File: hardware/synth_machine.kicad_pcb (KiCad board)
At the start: 2 copper layers, 100 x 100 mm, 93 parts, among them J1 USB-C (MIDI + 5V power), J10 Pot WAV (10k lin, panel) JST-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, J11 Pot ATK (10k lin, panel) JST-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, J12 Pot DEC (10k lin, panel) JST-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, J13 Pot SUS (10k lin, panel) JST-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, J14 Pot REL (10k lin, panel) JST-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, J5 Speaker L (JST-PH), J6 Speaker R (JST-PH), J7 Headphones 3.5mm (CUI SJ1-351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, J8 Expansion, K1 KEY C4 (direct D10) JST-XH, K10 A4 [c2 r2] JST-XH, K11 A#4 [c1 r1] JST-XH, K12 B4 [c1 r2] JST-XH, K13 C5 [c0 r2] JST-XH, K14 BTN1 [c0 r0] JST-XH, K15 BTN2 [c0 r1] JST-XH, K16 BTN3 [c1 r0] JST-XH, K17 BTN4 [c2 r0] JST-XH, K18 BTN5 [c3 r0] JST-XH, K19 BTN6 [c4 r0] JST-XH, K2 C#4 [c5 r0] JST-XH, K3 D4 [c5 r1] JST-XH, K4 D#4 [c4 r1] JST-XH, K5 E4 [c5 r2] JST-XH, K6 F4 [c4 r2] JST-XH, K7 F#4 [c3 r1] JST-XH, K8 G4 [c3 r2] JST-XH, K9 G#4 [c2 r1] JST-XH, Q1 MMBT3904, U1 Daisy Seed / Seed3, U2 TPA6138A2PWR, U3 MAX98306ETD+T

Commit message: v0.3 silkscreen: bottom-row key labels sit just above their diodes
Also gives the amp's +5V decoupling island a locked exit stub and via so the
autorouter can always reach it (it was boxed in by the speaker fan-out).

Co-Authored-By: Claude Fable 5.1 <noreply@anthropic.com>
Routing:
- net POT_WAVE: track 63.7 -> 89.2 mm, vias 1 -> 0
- net POT_RELEASE: track 88.0 -> 111.7 mm, vias 1 -> 0
- net HP_L: track 58.5 -> 39.6 mm
- net +3V3: track 108.4 -> 124.5 mm
- net +5V: track 153.4 -> 138.3 mm, vias 1 -> 3
- net KAs4_D: track 13.3 -> 28.2 mm, vias 1 -> 0
- net HP_INL: track 38.6 -> 25.1 mm, vias 0 -> 2
- net KCs4_D: track 7.17 -> 18.9 mm
- net GND: track 415.7 -> 407.4 mm
- net EXP_A5: track 47.6 -> 40.0 mm, vias 0 -> 1
- net ROW0: track 183.2 -> 189.2 mm
- net CC2: track 29.7 -> 23.9 mm
- net KBTN1_D: track 16.3 -> 22.0 mm
- net COL4: track 135.8 -> 130.9 mm
- net CC1: track 22.5 -> 18.3 mm, vias 2 -> 0
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
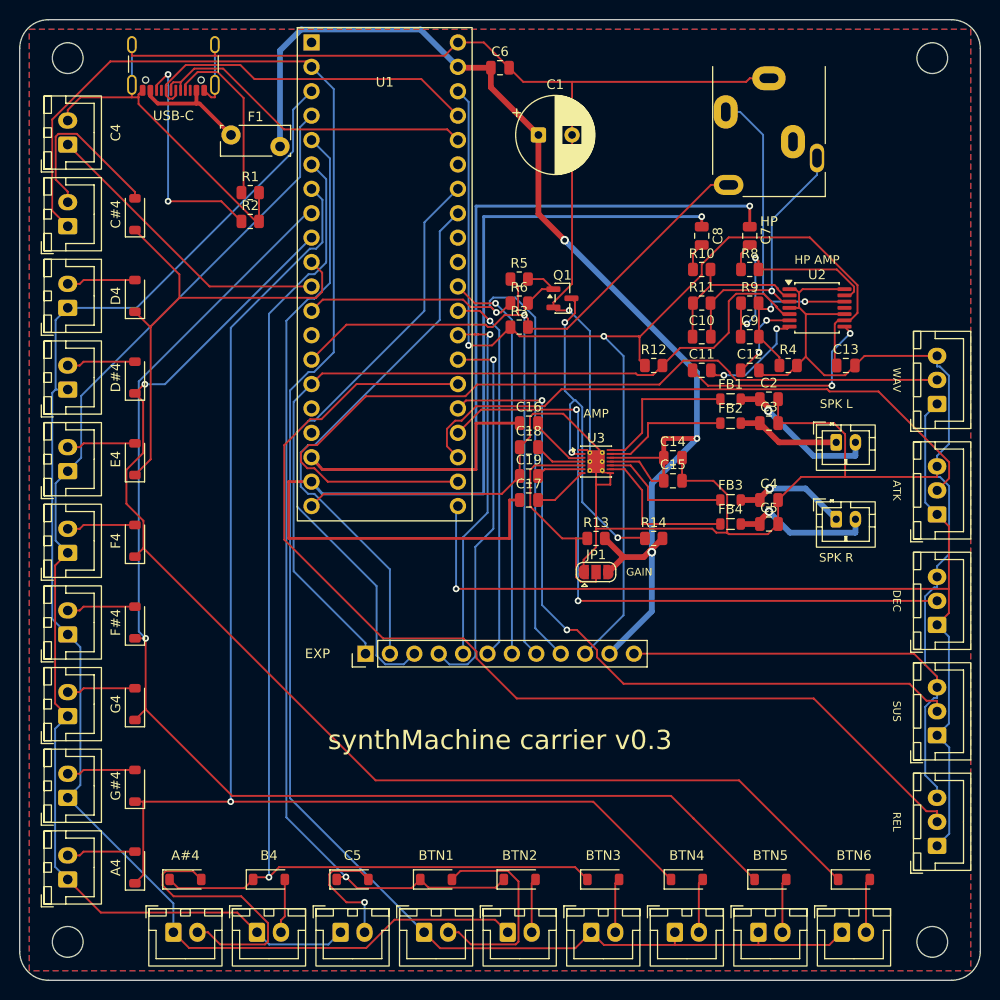
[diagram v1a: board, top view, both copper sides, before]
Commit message: J8 expansion header becomes a 1x12 female socket; Digi-Key list sized for two boards
Co-Authored-By: Claude Fable 5.1 <noreply@anthropic.com>
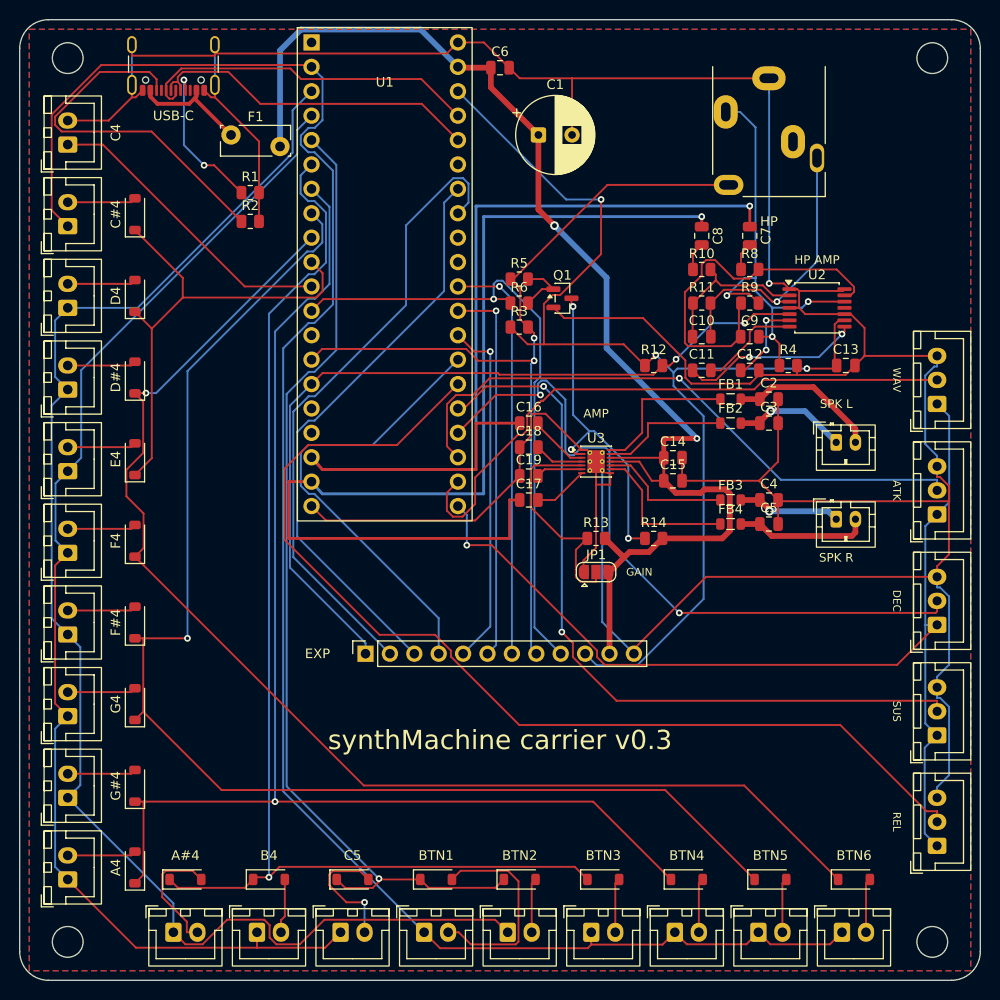
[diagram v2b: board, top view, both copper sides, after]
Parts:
- J8: value Expansion -> Expansion (1x12 female socket); footprint PinHeader_1x12_P2.54mm_Vertical -> PinSocket_1x12_P2.54mm_Vertical
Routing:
- net POT_WAVE: track 89.2 -> 63.2 mm
- net KAs4_D: track 28.2 -> 12.8 mm
- net CC2: track 23.9 -> 38.4 mm, vias 2 -> 0
- net HP_INL: track 25.1 -> 38.6 mm, vias 2 -> 0
- net KCs4_D: track 18.9 -> 7.17 mm
- net EXP_D26: track 57.3 -> 66.3 mm
- net EXP_A5: track 40.0 -> 47.6 mm, vias 1 -> 0
- net HP_L: track 39.6 -> 46.3 mm, vias 2 -> 3
- net AMP_SD: track 37.6 -> 33.4 mm
- net GND: track 407.4 -> 411.3 mm
- net +3V3: track 124.5 -> 120.8 mm, vias 2 -> 3
- net HP_CP: track 22.3 -> 18.8 mm
- net HP_MUTE: track 88.6 -> 85.2 mm, vias 0 -> 2
- net EXP_D27: track 64.1 -> 60.7 mm
- net POT_DECAY: track 70.7 -> 73.8 mm
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
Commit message: Keep the J8 pin-header footprint; Digi-Key list sized for two boards with female sockets for J8
Board files restored to the eda5d51 state (identical to what was uploaded to
JLCPCB); a 1x12 female socket solders into the same holes.

Co-Authored-By: Claude Fable 5.1 <noreply@anthropic.com>
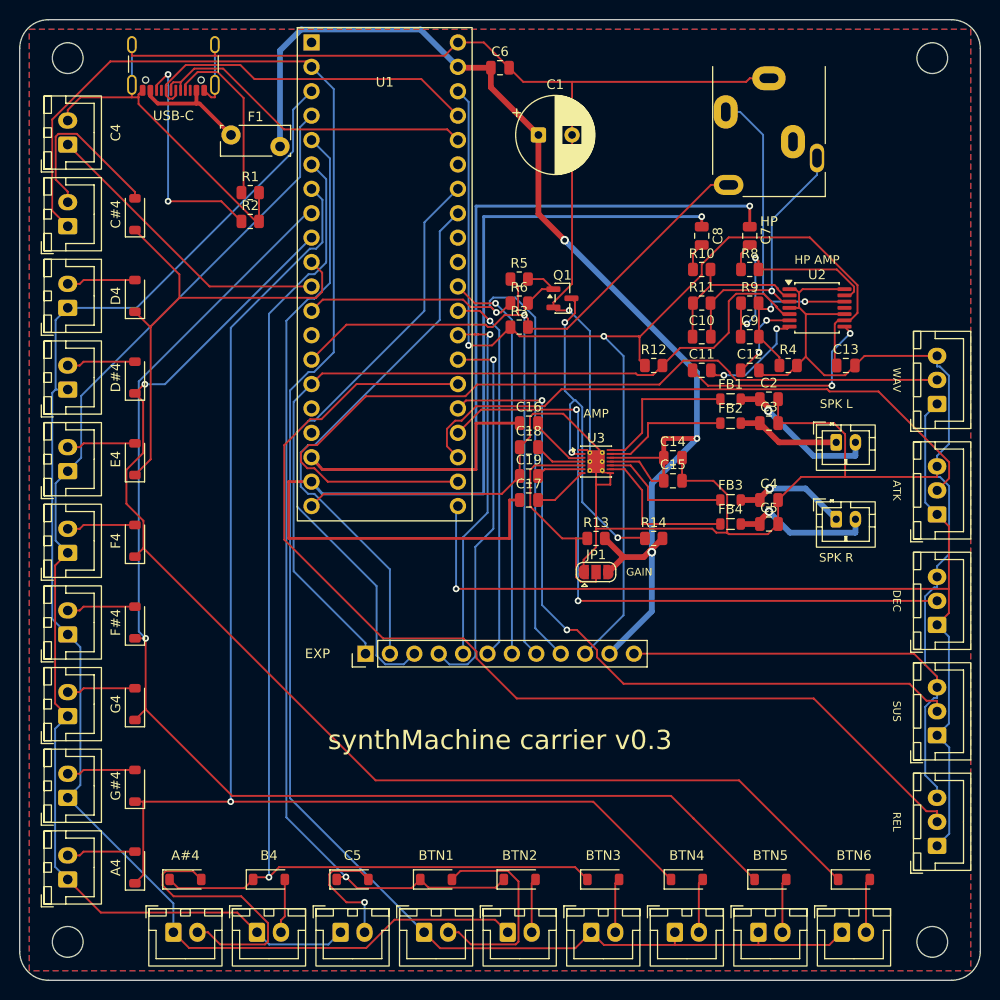
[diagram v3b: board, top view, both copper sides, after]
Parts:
- J8: value Expansion (1x12 female socket) -> Expansion; footprint PinSocket_1x12_P2.54mm_Vertical -> PinHeader_1x12_P2.54mm_Vertical
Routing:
- net POT_WAVE: track 63.2 -> 89.2 mm
- net KAs4_D: track 12.8 -> 28.2 mm
- net CC2: track 38.4 -> 23.9 mm, vias 0 -> 2
- net HP_INL: track 38.6 -> 25.1 mm, vias 0 -> 2
- net KCs4_D: track 7.17 -> 18.9 mm
- net EXP_D26: track 66.3 -> 57.3 mm
- net EXP_A5: track 47.6 -> 40.0 mm, vias 0 -> 1
- net HP_L: track 46.3 -> 39.6 mm, vias 3 -> 2
- net AMP_SD: track 33.4 -> 37.6 mm
- net GND: track 411.3 -> 407.4 mm
- net +3V3: track 120.8 -> 124.5 mm, vias 3 -> 2
- net HP_CP: track 18.8 -> 22.3 mm
- net HP_MUTE: track 85.2 -> 88.6 mm, vias 2 -> 0
- net EXP_D27: track 60.7 -> 64.1 mm
- net POT_DECAY: track 73.8 -> 70.7 mm
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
